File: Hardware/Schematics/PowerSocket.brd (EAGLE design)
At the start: 100 x 80 mm, 72 parts, among them T1 BT138-H, T2 BT138-H, T3 BT138-H, T4 BT138-H, T5 BT138-H, T6 BT138-H

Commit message: Fixed error in wiring of voltage divider.
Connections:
- removed net N$38: R25.1, R26.1
- removed net N$39 (its old number): R27.1, R28.1
- removed net N$40: R29.1, R30.1
- net AMP1: now also R27.1, R28.1; no longer R28.3
- net AMP2: now also R25.1, R26.1; no longer R26.3
- net AMP3: now also R29.1, R30.1; no longer R30.3
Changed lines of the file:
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@@
 <contactref element="C1" pad="2"/>
 <contactref element="C4" pad="2"/>
-<contactref element="R26" pad="2"/>
-<contactref element="R28" pad="2"/>
-<contactref element="R30" pad="2"/>
 <contactref element="U$1" pad="IN-"/>
 <contactref element="U$1" pad="GND"/>
 <contactref element="U$1" pad="D+"/>
 <contactref element="U$1" pad="D-"/>
+<contactref element="R30" pad="2"/>
+<contactref element="R26" pad="2"/>
+<contactref element="R28" pad="2"/>
 <wire x1="-74.295" y1="-55.88" x2="-92.075" y2="-61.595" width="0" layer="19" extent="1-1"/>
 <wire x1="-74.295" y1="-53.34" x2="-74.295" y2="-55.88" width="0" layer="19" extent="1-1"/>
@@
 <signal name="AMP3">
 <contactref element="ESP3212" pad="IO32"/>
-<contactref element="R30" pad="3"/>
-<wire x1="83" y1="31.4" x2="-87.75" y2="-35.02" width="0" layer="19" extent="1-1"/>
+<contactref element="R29" pad="1"/>
+<contactref element="R30" pad="1"/>
+<wire x1="-90.05" y1="-35.02" x2="-92.39" y2="-39.37" width="0" layer="19" extent="1-1"/>
+<wire x1="83" y1="31.4" x2="-90.05" y2="-35.02" width="0" layer="19" extent="1-1"/>
 </signal>
 <signal name="AMP2">
 <contactref element="ESP3212" pad="IO35"/>
-<contactref element="R26" pad="3"/>
-<wire x1="-87.75" y1="-15.97" x2="84.5" y2="31.4" width="0" layer="19" extent="1-1"/>
+<contactref element="R25" pad="1"/>
+<contactref element="R26" pad="1"/>
+<wire x1="-92.39" y1="-5.08" x2="84.5" y2="31.4" width="0" layer="19" extent="1-1"/>
+<wire x1="-90.05" y1="-15.97" x2="-92.39" y2="-5.08" width="0" layer="19" extent="1-1"/>
 </signal>
 <signal name="AMP1">
 <contactref element="ESP3212" pad="IO34"/>
-<contactref element="R28" pad="3"/>
-<wire x1="-87.75" y1="-22.32" x2="86" y2="31.4" width="0" layer="19" extent="1-1"/>
+<contactref element="R27" pad="1"/>
+<contactref element="R28" pad="1"/>
+<wire x1="-90.05" y1="-22.32" x2="-92.39" y2="-26.67" width="0" layer="19" extent="1-1"/>
+<wire x1="86" y1="31.4" x2="-90.05" y2="-22.32" width="0" layer="19" extent="1-1"/>
 </signal>
 <signal name="N$66">
@@
 </polygon>
 </signal>
-<signal name="N$37">
-<contactref element="AMP2" pad="7"/>
-<contactref element="R25" pad="2"/>
-<wire x1="38.365" y1="30.4" x2="-90.49" y2="-5.08" width="0" layer="19" extent="1-16"/>
-</signal>
-<signal name="N$38">
-<contactref element="R25" pad="1"/>
-<contactref element="R26" pad="1"/>
-<wire x1="-92.39" y1="-5.08" x2="-90.05" y2="-15.97" width="0" layer="19" extent="1-1"/>
-</signal>
-<signal name="N$39">
-<contactref element="R27" pad="1"/>
-<contactref element="R28" pad="1"/>
-<wire x1="-90.05" y1="-22.32" x2="-92.39" y2="-26.67" width="0" layer="19" extent="1-1"/>
-</signal>
-<signal name="N$40">
-<contactref element="R29" pad="1"/>
-<contactref element="R30" pad="1"/>
-<wire x1="-90.05" y1="-35.02" x2="-92.39" y2="-39.37" width="0" layer="19" extent="1-1"/>
-</signal>
-<signal name="N$43">
-<contactref element="AMP3" pad="7"/>
-<contactref element="R29" pad="2"/>
-<wire x1="16.365" y1="30.4" x2="-90.49" y2="-39.37" width="0" layer="19" extent="1-16"/>
-</signal>
 <signal name="+5V">
 <contactref element="U$1" pad="5V"/>
@@
 <wire x1="-82.23" y1="87.63" x2="-69.53" y2="87.63" width="0" layer="19" extent="1-1"/>
 </signal>
-<signal name="N$44">
+<signal name="N$37">
+<contactref element="AMP3" pad="7"/>
+<contactref element="R29" pad="2"/>
+<wire x1="16.365" y1="30.4" x2="-90.49" y2="-39.37" width="0" layer="19" extent="1-16"/>
+</signal>
+<signal name="N$39">
+<contactref element="AMP2" pad="7"/>
+<contactref element="R25" pad="2"/>
+<wire x1="38.365" y1="30.4" x2="-90.49" y2="-5.08" width="0" layer="19" extent="1-16"/>
+</signal>
+<signal name="N$41">
 <contactref element="AMP1" pad="7"/>
 <contactref element="R27" pad="2"/>

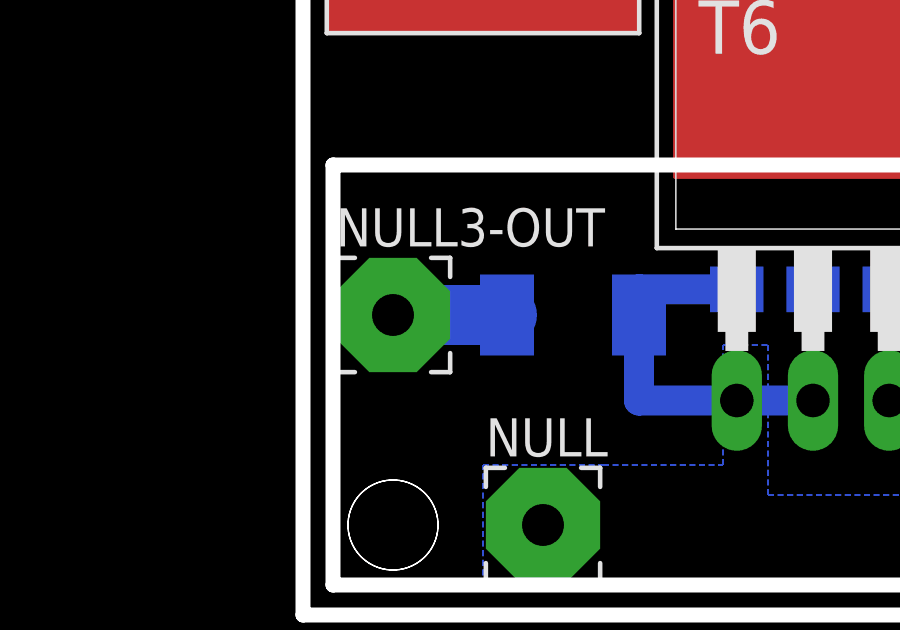
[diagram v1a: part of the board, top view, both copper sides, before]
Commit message: Fixed triac wiring.
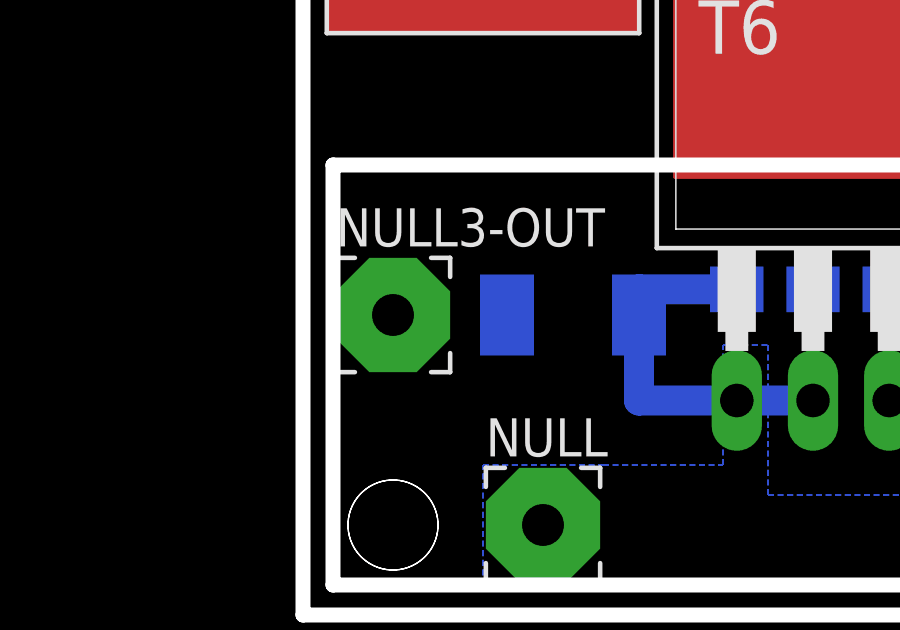
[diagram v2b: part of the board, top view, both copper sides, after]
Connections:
- removed net N$14: NULL2-OUT.1, R13.2, T4.T2
- new net NULL_: NULL3-OUT.1, T6.T1
- net N$17: now also NULL2-OUT.1, T4.T1; no longer NULL1-OUT.1, R4.2, T2.T2
- net N$8: now also NULL1-OUT.1, T2.T1; no longer NULL3-OUT.1, R17.2, T6.T2
- net NULL: now also R13.2, R17.2, R4.2, T2.T2, T4.T2, T6.T2; no longer T2.T1, T4.T1, T6.T1
- net PHASE: now also R10.2, R15.2, R19.2, T1.T2, T3.T2, T5.T2; no longer T1.T1, T3.T1, T5.T1
- net PHASE1: now also T1.T1; no longer R10.2, T1.T2
- net PHASE2: now also T3.T1; no longer R15.2, T3.T2
- net PHASE3: now also T5.T1; no longer R19.2, T5.T2
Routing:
- net N$8: track 12.4 -> 0.00 mm
- net NULL: track 0.00 -> 8.65 mm
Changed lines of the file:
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@@
 <contactref element="AMP1" pad="2"/>
 <contactref element="AMP1" pad="1"/>
-<contactref element="R10" pad="2"/>
-<contactref element="T1" pad="T2"/>
-<wire x1="60.365" y1="35.6" x2="60.2" y2="41" width="0" layer="19" extent="16-16"/>
+<contactref element="T1" pad="T1"/>
 <wire x1="59.095" y1="35.6" x2="60.365" y2="35.6" width="0" layer="19" extent="16-16"/>
-<wire x1="50" y1="40.35" x2="60.2" y2="41" width="0" layer="19" extent="16-16"/>
+<wire x1="52.54" y1="40.35" x2="59.095" y2="35.6" width="0" layer="19" extent="16-16"/>
 </signal>
 <signal name="N$27">
@@
 <wire x1="63.54" y1="7.15" x2="63.54" y2="10.855" width="0" layer="19" extent="16-16"/>
 </signal>
-<signal name="N$17">
-<contactref element="R4" pad="2"/>
-<contactref element="NULL1-OUT" pad="1"/>
-<contactref element="T2" pad="T2"/>
-<wire x1="50.8" y1="10" x2="61" y2="7.15" width="0" layer="19" extent="16-16"/>
-<wire x1="47" y1="10" x2="50.8" y2="10" width="0" layer="19" extent="16-16"/>
-</signal>
 <signal name="N$19">
 <contactref element="OK1" pad="4"/>
@@
 </signal>
 <signal name="PHASE">
-<contactref element="T1" pad="T1"/>
 <contactref element="PHASE" pad="1"/>
-<contactref element="T3" pad="T1"/>
-<contactref element="T5" pad="T1"/>
 <contactref element="D1" pad="C"/>
-<wire x1="30.54" y1="40.35" x2="52.54" y2="40.35" width="0" layer="19" extent="1-1"/>
-<wire x1="8.54" y1="40.35" x2="30.54" y2="40.35" width="0" layer="19" extent="1-1"/>
-<wire x1="8" y1="44.5" x2="8.54" y2="40.35" width="0" layer="19" extent="1-1"/>
+<contactref element="R19" pad="2"/>
+<contactref element="T5" pad="T2"/>
+<contactref element="R10" pad="2"/>
+<contactref element="T1" pad="T2"/>
+<contactref element="R15" pad="2"/>
+<contactref element="T3" pad="T2"/>
+<wire x1="50" y1="40.35" x2="60.2" y2="41" width="0" layer="19" extent="16-16"/>
+<wire x1="38.2" y1="41" x2="50" y2="40.35" width="0" layer="19" extent="16-16"/>
+<wire x1="28" y1="40.35" x2="38.2" y2="41" width="0" layer="19" extent="16-16"/>
+<wire x1="16.2" y1="41" x2="28" y2="40.35" width="0" layer="19" extent="16-16"/>
+<wire x1="8" y1="44.5" x2="16.2" y2="41" width="0" layer="19" extent="16-16"/>
+<wire x1="6" y1="40.35" x2="8" y2="44.5" width="0" layer="19" extent="1-1"/>
 <wire x1="-36.83" y1="87.63" x2="8" y2="44.5" width="0" layer="19" extent="1-1"/>
 </signal>
 <signal name="NULL">
-<contactref element="T2" pad="T1"/>
 <contactref element="NULL" pad="1"/>
 <contactref element="R5" pad="1"/>
-<contactref element="T4" pad="T1"/>
-<contactref element="T6" pad="T1"/>
-<wire x1="64.8" y1="2" x2="58.46" y2="7.15" width="0" layer="19" extent="16-16"/>
-<wire x1="36.46" y1="7.15" x2="58.46" y2="7.15" width="0" layer="19" extent="1-1"/>
-<wire x1="14.46" y1="7.15" x2="36.46" y2="7.15" width="0" layer="19" extent="1-1"/>
-<wire x1="8" y1="3" x2="14.46" y2="7.15" width="0" layer="19" extent="1-1"/>
-</signal>
-<signal name="N$14">
+<contactref element="R17" pad="2"/>
+<contactref element="T6" pad="T2"/>
+<wire x1="17" y1="7.15" x2="11.2" y2="7.15" width="1" layer="16"/>
+<wire x1="11.2" y1="7.15" x2="11.2" y2="10" width="1" layer="16"/>
+<contactref element="R4" pad="2"/>
+<contactref element="T2" pad="T2"/>
 <contactref element="R13" pad="2"/>
-<contactref element="NULL2-OUT" pad="1"/>
 <contactref element="T4" pad="T2"/>
+<wire x1="64.8" y1="2" x2="61" y2="7.15" width="0" layer="19" extent="16-16"/>
+<wire x1="50.8" y1="10" x2="61" y2="7.15" width="0" layer="19" extent="16-16"/>
+<wire x1="39" y1="7.15" x2="50.8" y2="10" width="0" layer="19" extent="16-16"/>
 <wire x1="28.8" y1="10" x2="39" y2="7.15" width="0" layer="19" extent="16-16"/>
-<wire x1="25" y1="10" x2="28.8" y2="10" width="0" layer="19" extent="16-16"/>
+<wire x1="17" y1="7.15" x2="28.8" y2="10" width="0" layer="19" extent="16-16"/>
+<wire x1="6.8" y1="10" x2="11.2" y2="10" width="0" layer="19" extent="16-16"/>
+<wire x1="8" y1="3" x2="11.2" y2="7.15" width="0" layer="19" extent="16-16"/>
 </signal>
 <signal name="N$16">
@@
 </signal>
 <signal name="PHASE2">
-<contactref element="R15" pad="2"/>
-<contactref element="T3" pad="T2"/>
 <contactref element="AMP2" pad="2"/>
 <contactref element="AMP2" pad="1"/>
-<wire x1="38.365" y1="35.6" x2="38.2" y2="41" width="0" layer="19" extent="16-16"/>
+<contactref element="T3" pad="T1"/>
 <wire x1="37.095" y1="35.6" x2="38.365" y2="35.6" width="0" layer="19" extent="16-16"/>
-<wire x1="28" y1="40.35" x2="38.2" y2="41" width="0" layer="19" extent="16-16"/>
+<wire x1="30.54" y1="40.35" x2="37.095" y2="35.6" width="0" layer="19" extent="16-16"/>
 </signal>
 <signal name="PHASE3">
-<contactref element="R19" pad="2"/>
-<contactref element="T5" pad="T2"/>
 <contactref element="AMP3" pad="2"/>
 <contactref element="AMP3" pad="1"/>
-<wire x1="16.365" y1="35.6" x2="16.2" y2="41" width="0" layer="19" extent="16-16"/>
+<contactref element="T5" pad="T1"/>
 <wire x1="15.095" y1="35.6" x2="16.365" y2="35.6" width="0" layer="19" extent="16-16"/>
-<wire x1="6" y1="40.35" x2="16.2" y2="41" width="0" layer="19" extent="16-16"/>
-</signal>
-<signal name="N$8">
-<contactref element="NULL3-OUT" pad="1"/>
-<contactref element="R17" pad="2"/>
-<contactref element="T6" pad="T2"/>
-<wire x1="17" y1="7.15" x2="11.2" y2="7.15" width="1" layer="16"/>
-<wire x1="11.2" y1="7.15" x2="11.2" y2="10" width="1" layer="16"/>
-<wire x1="6.8" y1="10" x2="3" y2="10" width="2" layer="16"/>
-<wire x1="6.8" y1="10" x2="11.2" y2="10" width="0" layer="19" extent="16-16"/>
+<wire x1="8.54" y1="40.35" x2="15.095" y2="35.6" width="0" layer="19" extent="16-16"/>
 </signal>
 <signal name="N$18">
@@
 <wire x1="60.365" y1="30.4" x2="-90.49" y2="-26.67" width="0" layer="19" extent="1-16"/>
 </signal>
+<signal name="NULL_">
+<contactref element="NULL3-OUT" pad="1"/>
+<contactref element="T6" pad="T1"/>
+<wire x1="3" y1="10" x2="14.46" y2="7.15" width="0" layer="19" extent="1-1"/>
+</signal>
+<signal name="N$8">
+<contactref element="NULL1-OUT" pad="1"/>
+<contactref element="T2" pad="T1"/>
+<wire x1="47" y1="10" x2="58.46" y2="7.15" width="0" layer="19" extent="1-1"/>
+</signal>
+<signal name="N$17">
+<contactref element="NULL2-OUT" pad="1"/>
+<contactref element="T4" pad="T1"/>
+<wire x1="25" y1="10" x2="36.46" y2="7.15" width="0" layer="19" extent="1-1"/>
+</signal>
 </signals>

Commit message: Changed resistor values.
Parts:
- R10, R13, R15, R17, R19, R4: value 150 -> 300
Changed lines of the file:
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@@
 <element name="PHASE3-OUT" library="wirepad" package="3,81/1,4" value="-" x="20" y="41"/>
 <element name="R1" library="rcl" package="R0805" value="10K" x="86.5" y="39" rot="R180"/>
-<element name="R10" library="eagle-ltspice" package="R2010" value="150" x="58" y="41" rot="MR180">
+<element name="R10" library="eagle-ltspice" package="R2010" value="300" x="58" y="41" rot="MR180">
 <attribute name="SPICEPREFIX" value="R" x="58" y="41" size="1.778" layer="28" rot="MR180" display="off"/>
 <attribute name="SPICEMODEL" value="NONE" x="58" y="41" size="1.778" layer="28" rot="MR180" display="off"/>
@@
 <element name="R11" library="rcl" package="R0805" value="10K" x="77.5" y="21"/>
 <element name="R12" library="rcl" package="R0805" value="150" x="39" y="23.5" rot="MR270"/>
-<element name="R13" library="eagle-ltspice" package="R2010" value="150" x="31" y="10" rot="MR0">
+<element name="R13" library="eagle-ltspice" package="R2010" value="300" x="31" y="10" rot="MR0">
 <attribute name="SPICEPREFIX" value="R" x="31" y="10" size="1.778" layer="28" rot="MR0" display="off"/>
 <attribute name="SPICEMODEL" value="NONE" x="31" y="10" size="1.778" layer="28" rot="MR0" display="off"/>
 </element>
 <element name="R14" library="rcl" package="R0805" value="150" x="28" y="24" rot="MR270"/>
-<element name="R15" library="eagle-ltspice" package="R2010" value="150" x="36" y="41" rot="MR180">
+<element name="R15" library="eagle-ltspice" package="R2010" value="300" x="36" y="41" rot="MR180">
 <attribute name="SPICEPREFIX" value="R" x="36" y="41" size="1.778" layer="28" rot="MR180" display="off"/>
 <attribute name="SPICEMODEL" value="NONE" x="36" y="41" size="1.778" layer="28" rot="MR180" display="off"/>
 </element>
 <element name="R16" library="rcl" package="R0805" value="150" x="17" y="23.5" rot="MR270"/>
-<element name="R17" library="eagle-ltspice" package="R2010" value="150" x="9" y="10" rot="MR0">
+<element name="R17" library="eagle-ltspice" package="R2010" value="300" x="9" y="10" rot="MR0">
 <attribute name="SPICEPREFIX" value="R" x="9" y="10" size="1.778" layer="28" rot="MR0" display="off"/>
 <attribute name="SPICEMODEL" value="NONE" x="9" y="10" size="1.778" layer="28" rot="MR0" display="off"/>
 </element>
 <element name="R18" library="rcl" package="R0805" value="150" x="6" y="24" rot="MR90"/>
-<element name="R19" library="eagle-ltspice" package="R2010" value="150" x="14" y="41" rot="MR180">
+<element name="R19" library="eagle-ltspice" package="R2010" value="300" x="14" y="41" rot="MR180">
 <attribute name="SPICEPREFIX" value="R" x="14" y="41" size="1.778" layer="28" rot="MR180" display="off"/>
 <attribute name="SPICEMODEL" value="NONE" x="14" y="41" size="1.778" layer="28" rot="MR180" display="off"/>
@@
 <element name="R23" library="rcl" package="R0805" value="10K" x="80" y="19" rot="MR90"/>
 <element name="R3" library="rcl" package="R0805" value="150" x="61" y="23.5" rot="MR90"/>
-<element name="R4" library="eagle-ltspice" package="R2010" value="150" x="53" y="10" rot="MR0">
+<element name="R4" library="eagle-ltspice" package="R2010" value="300" x="53" y="10" rot="MR0">
 <attribute name="SPICEPREFIX" value="R" x="53" y="10" size="1.778" layer="28" rot="MR0" display="off"/>
 <attribute name="SPICEMODEL" value="NONE" x="53" y="10" size="1.778" layer="28" rot="MR0" display="off"/>

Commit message: Replaced triacs with realys Replaced ESP3212 with ESP-12S
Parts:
- removed ESP3212: ESP3212LABELS, esp3212-ptw:ESP3212
- removed OK1, OK2, OK3, OK4, OK5, OK6: MOC3041S, optocoupler:DIL6-SMD
- removed R10, R13, R15, R17, R19: 300, eagle-ltspice:R2010
- removed R12, R14, R16, R18: 150, rcl:R0805
- removed T1, T2, T3, T4, T5, T6: BT138-H, triac:TO220BH
- added Q1, Q2, Q3: (no value), adafruit:SOT23
- added U$2, U$3, U$4, U$5, U$6, U$7: RELAYPTH, SRD-05VDC-SL-C:SRD-05VDC-SL-C
- added U1: ESP-32S, esp32:ESP-32S
- R3, R9: value 150 -> 100
- R4: value 300 -> 100; device eagle-ltspice:R2010 -> rcl:R0805
- moved R9 259.1 mm to (-91.4, -193.0), flipped to the top, turned to 0 degrees
- moved R4 244.0 mm to (-91.4, -186.7), flipped to the top
- moved R3 182.1 mm to (-91.4, -76.2), flipped to the top, turned to 0 degrees
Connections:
- removed net N$19: OK1.4, T1.G
- removed net N$20: OK1.6, R10.1
- removed net N$21: OK2.6, R4.1
- removed net N$22: OK4.4, T4.G
- removed net N$23: OK3.6, R15.1
- removed net N$25: OK3.4, T3.G
- removed net N$28: OK3.2, R14.1
- removed net N$29: OK4.2, R12.2
- removed net N$31: OK6.2, R16.2
- removed net N$33: OK6.6, R17.1
- removed net N$34: OK6.4, T6.G
- removed net N$35: OK5.6, R19.1
- removed net N$36: OK5.4, T5.G
- new net N$14: Q2.1, R4.1
- net AMP1: now also U1.6; no longer ESP3212.IO34
- net AMP2: now also U1.7; no longer ESP3212.IO35
- net AMP3: now also U1.8; no longer ESP3212.IO32
- net BUTTON1: now also U1.33; no longer ESP3212.IO22
- net BUTTON2: now also U1.30; no longer ESP3212.IO23
- net BUTTON3: now also U1.28; no longer ESP3212.IO5
- net FLASH: now also U1.10; no longer ESP3212.IO25
- net GATE1: now also U1.25; no longer ESP3212.IO0, R9.2
- net GATE2: now also R4.2, U1.26; no longer ESP3212.IO4, R12.1, R14.2
- net GATE3: now also R9.2, U1.37; no longer ESP3212.IO16, R16.1, R18.1
- net GND: now also U$2.COIL0, U$3.COIL0, U$4.COIL0, U$5.COIL0, U$6.COIL0, U$7.COIL0, U1.1, U1.15, U1.24, U1.38, U1.GND; no longer ESP3212.GND_B, ESP3212.GND_L, ESP3212.GND_R, ESP3212.IO2
- net LED1: now also U1.31; no longer ESP3212.IO19
- net LED2: now also U1.29; no longer ESP3212.IO18
- net LED3: now also U1.27; no longer ESP3212.IO17
- net N$1: now also Q1.1, R3.1; no longer OK1.2, R9.1
- net N$15: now also Q2.2, U$4.COIL1, U$5.COIL1; no longer OK2.4, T2.G
- net N$16: now also Q3.1, R9.1; no longer OK4.6, R13.1
- net N$17: now also U$5.SWOPEN; no longer T4.T1
- net N$18: now also Q3.2, U$6.COIL1, U$7.COIL1; no longer OK5.2, R18.2
- net N$2: now also U1.23; no longer ESP3212.IO15
- net N$3: now also U1.16; no longer ESP3212.IO13
- net N$4: now also U1.14; no longer ESP3212.IO12
- net N$5: now also U1.13; no longer ESP3212.IO14
- net N$6: now also Q1.2, U$2.COIL1, U$3.COIL1; no longer OK2.2, R3.1
- net N$66: now also U1.3; no longer ESP3212.EN
- net N$70: now also U1.35; no longer ESP3212.U0TX
- net N$77: now also U1.34; no longer ESP3212.U0RX
- net N$8: now also U$3.SWOPEN; no longer T2.T1
- net NULL: now also U$3.SWCOMMON, U$5.SWCOMMON, U$7.SWCOMMON; no longer R13.2, R17.2, R4.2, T2.T2, T4.T2, T6.T2
- net NULL_: now also U$7.SWOPEN; no longer T6.T1
- net PHASE: now also U$2.SWCOMMON, U$4.SWCOMMON, U$6.SWCOMMON; no longer R10.2, R15.2, R19.2, T1.T2, T3.T2, T5.T2
- net PHASE1: now also U$2.SWOPEN; no longer T1.T1
- net PHASE2: now also U$4.SWOPEN; no longer T3.T1
- net PHASE3: now also U$6.SWOPEN; no longer T5.T1
- net VCC: now also Q1.3, Q2.3, Q3.3, U1.2; no longer ESP3212.3V3, OK1.1, OK2.1, OK3.1, OK4.1, OK5.1, OK6.1
- net VOLTMETER: now also U1.11; no longer ESP3212.IO26
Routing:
- net NULL: track 8.65 -> 0.00 mm
- net N$33: track 4.12 -> 0.00 mm

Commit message: Small edits.
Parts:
- moved U1 280.4 mm to (85.1, 25.4), turned to 270 degrees
- moved U$6 217.0 mm to (11.4, 39.4)
- moved U$7 203.4 mm to (8.89, 10.2), turned to 270 degrees
- moved U$4 198.2 mm to (36.8, 38.1)
- moved U$2 189.8 mm to (57.1, 38.1)
- moved U$5 180.3 mm to (24.1, 10.2), turned to 270 degrees
- moved U$3 168.1 mm to (39.4, 10.2), turned to 270 degrees
- moved Q1 164.1 mm to (45.7, 19.1), flipped to the bottom
- moved NULL1-OUT 9.92 mm to (39.4, 3.65)
- moved NULL3-OUT 8.13 mm to (8.08, 3.65)
- moved NULL 7.62 mm to (8.00, 10.6)
- moved NULL2-OUT 6.48 mm to (23.7, 3.65)
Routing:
- removed copper zone on layer 16, net N$30
- removed copper zone on layer 16, net N$32
